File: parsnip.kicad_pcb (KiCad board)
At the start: 4 copper layers, 60 x 130 mm, 471 parts, among them J1 SPI0, J10 SOLAR, J11 SMA-KE-347-H13.5-1.6, J12 U.FL, J13 SMA-KE-347-H13.5-1.6, J14 GPIO_Expander, J15 LED 5V, J16 I2C3, J2 I2C4, J3 I2C1, J4 I2C2, J5 SPI1, J6 UART0, J7 USB4105-GF-A-060, J8 PD_I2C DEBUG, J9 BAT_PORT, Q1 CSD23280F3, Q10 SI2308, Q11 CSD17577Q3A, Q14 2N7002, Q15 2N7002, Q16 TPN2R203NC, Q2 CSD15380F3, Q3 CSD23280F3, Q4 CSD15380F3, Q5 AON7544, Q6 AON7544, Q7 CSD18512Q5B, Q8 CSD18512Q5B, Q9 SI2308, SW1 ESP_RESET, SW2 BOOT, SW3 RESET, SW4 RESET_GNSS, SW5 SAFEBOOT_GNSS, U1 ESP32-S3-WROOM-1-N16R8, U10 TPS7A2033PDBVR, U11 TPS259474LRPWR, U12 E22P-915M30S, U13 LM61460AASQRJRRQ1, U14 LM61460AASQRJRRQ1, U15 TPS259474ARPWR, U16 SN74LVC1G74, U17 TCAL9539RTWRQ1, U18 WS2816B, U19 SN74LV1T34DCK, U2 QMC6309, U20 WS2816B, U21 M24512-DFMC6TG, U22 LSM6DSV16X, U23 TPS22945DCKR, U24 TPD2E2U06QDCKRQ1, U3 TVS2200DRV, U4 TPD8S300A, U5 TPS25751DREFR, U6 TPS22945DCKR, U7 MAX17320G22+, U8 BQ25798, U9 NEO-F10N, Y1 32.768kHz, Y2 SX1M4.000M10F30TNN

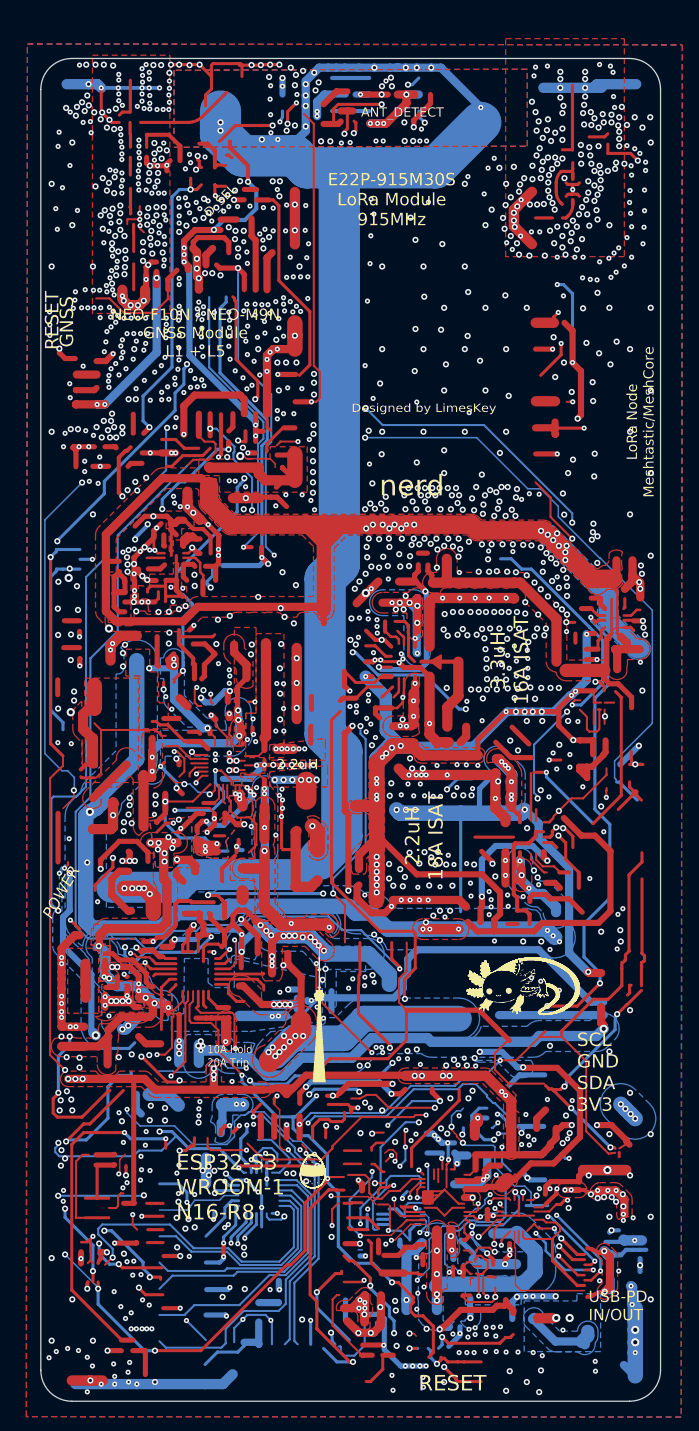
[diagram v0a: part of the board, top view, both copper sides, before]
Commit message: board: trace-quality pass 2 (checkpoint before pass 3)
Co-Authored-By: Claude Opus 5.5 <noreply@anthropic.com>
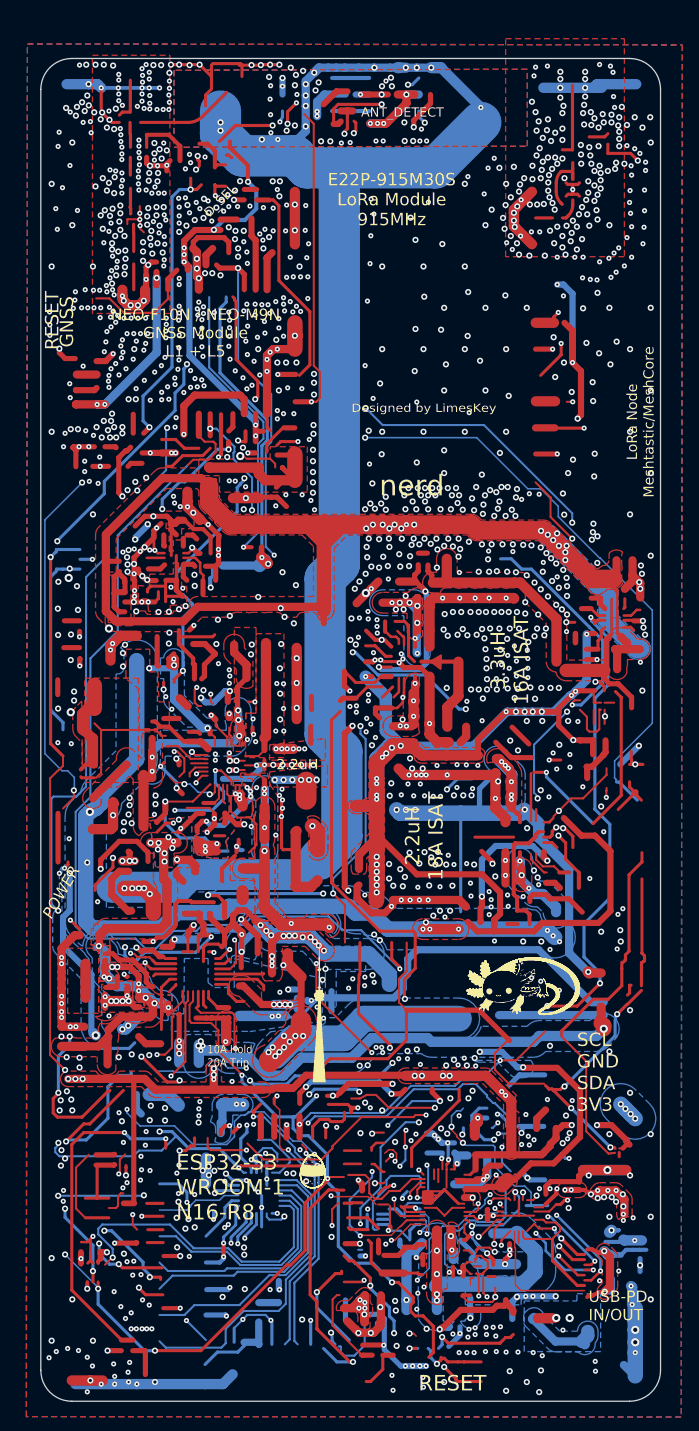
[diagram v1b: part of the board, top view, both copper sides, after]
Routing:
- net MOSI: track 179.3 -> 149.0 mm
- net Net-(Q11-G): track 17.2 -> 9.70 mm
- net I2C_HOST_SCL: track 260.6 -> 257.1 mm
- net Net-(U11-PGTH/~{FLT}): track 5.01 -> 1.86 mm
- net Net-(D22-A): track 6.87 -> 4.72 mm
- net Net-(U7-BATTS): track 14.5 -> 12.7 mm
- net /Root/LoRa/RESET: track 115.4 -> 114.1 mm
- net /Root/LoRa/ANT_DETECT: track 57.4 -> 56.4 mm
- net /Root/Connectors/UART0_TX_RAW: track 12.0 -> 11.1 mm
- net Net-(U8-TS): track 17.6 -> 16.8 mm
- net Net-(D23-COM): track 33.5 -> 32.8 mm
